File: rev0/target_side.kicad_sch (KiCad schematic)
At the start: 12 parts, among them IC1 ECP5-BGA256, U9 USB3343-CP

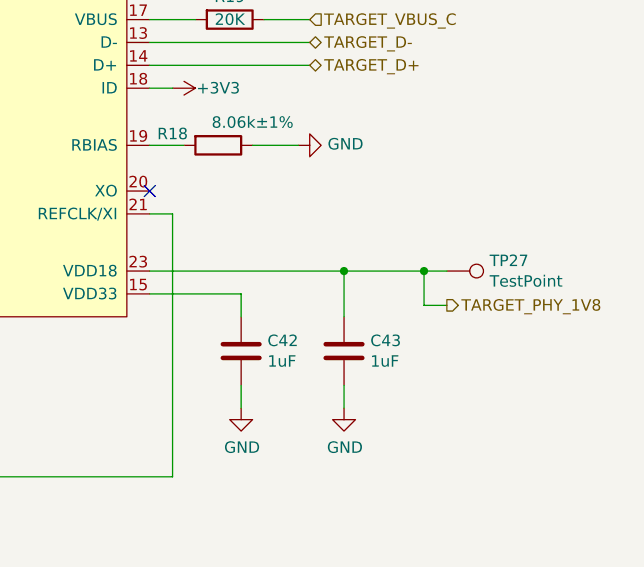
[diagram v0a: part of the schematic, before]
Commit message: hardware: remove PHY 1.8 V measurement
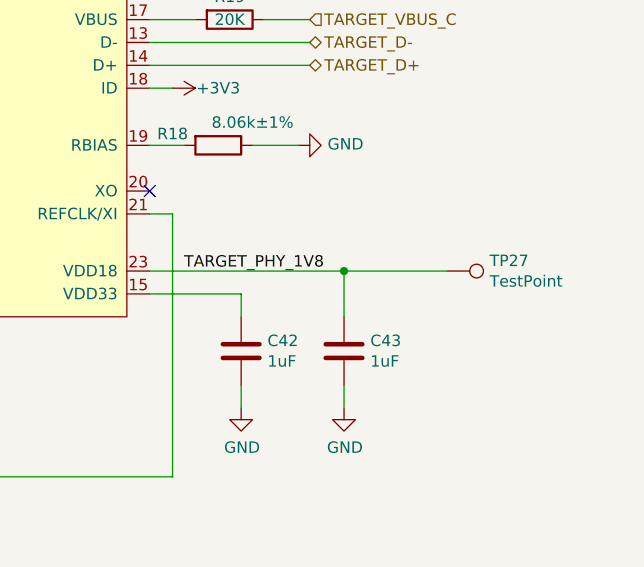
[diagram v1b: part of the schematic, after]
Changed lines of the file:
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@@
   (junction (at 123.19 66.04) (diameter 0) (color 0 0 0 0)
-  )
-  (junction (at 256.54 91.44) (diameter 0) (color 0 0 0 0)
   )
   (no_connect (at 59.69 99.06))
@@
     (stroke (width 0) (type default) (color 0 0 0 0))
   )
-  (wire (pts (xy 256.54 95.25) (xy 256.54 91.44))
-    (stroke (width 0) (type default) (color 0 0 0 0))
-  )
   (wire (pts (xy 59.69 91.44) (xy 137.16 91.44))
     (stroke (width 0) (type default) (color 0 0 0 0))
@@
     (stroke (width 0) (type default) (color 0 0 0 0))
   )
-  (wire (pts (xy 256.54 91.44) (xy 259.08 91.44))
-    (stroke (width 0) (type default) (color 0 0 0 0))
-  )
   (wire (pts (xy 59.69 124.46) (xy 137.16 124.46))
     (stroke (width 0) (type default) (color 0 0 0 0))
@@
     (stroke (width 0) (type default) (color 0 0 0 0))
   )
-  (wire (pts (xy 259.08 95.25) (xy 256.54 95.25))
-    (stroke (width 0) (type default) (color 0 0 0 0))
-  )
   (wire (pts (xy 226.06 91.44) (xy 247.65 91.44))
     (stroke (width 0) (type default) (color 0 0 0 0))
@@
     (stroke (width 0) (type default) (color 0 0 0 0))
   )
-  (wire (pts (xy 247.65 91.44) (xy 256.54 91.44))
+  (wire (pts (xy 247.65 91.44) (xy 259.08 91.44))
     (stroke (width 0) (type default) (color 0 0 0 0))
   )
@@
     (effects (font (size 1.27 1.27)) (justify left bottom))
   )
+  (label "TARGET_PHY_1V8" (at 229.87 91.44 0)
+    (effects (font (size 1.27 1.27)) (justify left bottom))
+  )
   (label "TARGET_DIR" (at 167.64 81.28 0)
     (effects (font (size 1.27 1.27)) (justify left bottom))
@@
     (effects (font (size 1.27 1.27)) (justify left))
   )
-  (hierarchical_label "TARGET_PHY_1V8" (shape output) (at 259.08 95.25 0)
-    (effects (font (size 1.27 1.27)) (justify left))
-  )

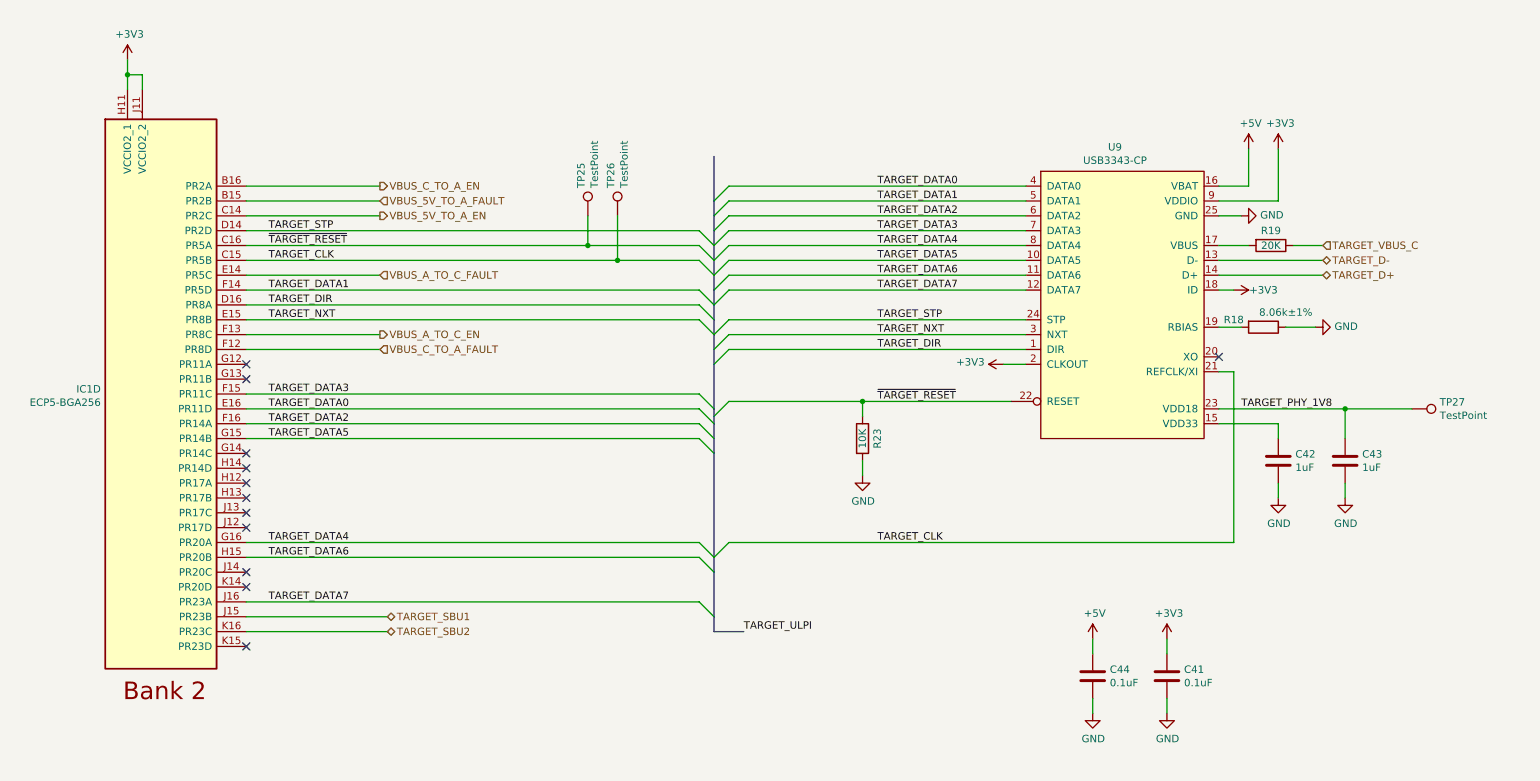
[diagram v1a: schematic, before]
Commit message: hardware: rename buses for KiCad 6
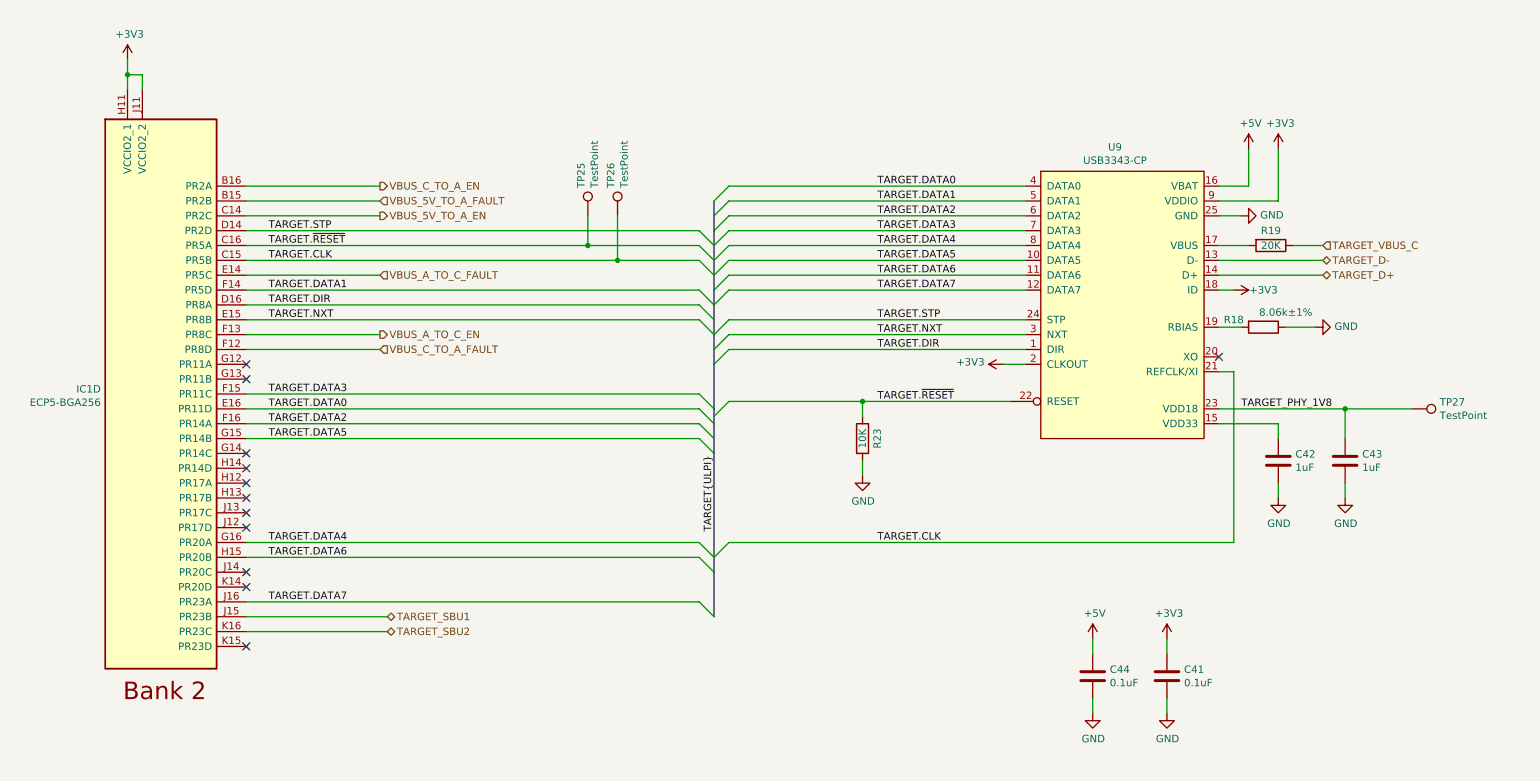
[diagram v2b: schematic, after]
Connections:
- net TARGET_CLK renamed TARGET.CLK
- net TARGET_DATA0 renamed TARGET.DATA0
- net TARGET_DATA1 renamed TARGET.DATA1
- net TARGET_DATA2 renamed TARGET.DATA2
- net TARGET_DATA3 renamed TARGET.DATA3
- net TARGET_DATA4 renamed TARGET.DATA4
- net TARGET_DATA5 renamed TARGET.DATA5
- net TARGET_DATA6 renamed TARGET.DATA6
- net TARGET_DATA7 renamed TARGET.DATA7
- net TARGET_DIR renamed TARGET.DIR
- net TARGET_NXT renamed TARGET.NXT
- net TARGET_STP renamed TARGET.STP
- net ~{TARGET_RESET} renamed TARGET.~{RESET}
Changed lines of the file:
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@@
-    (stroke (width 0) (type default) (color 0 0 0 0))
-  )
-  (bus (pts (xy 139.7 127) (xy 139.7 129.54))
     (stroke (width 0) (type default) (color 0 0 0 0))
   )
@@
     (stroke (width 0) (type default) (color 0 0 0 0))
   )
-  (bus (pts (xy 139.7 129.54) (xy 144.78 129.54))
-    (stroke (width 0) (type default) (color 0 0 0 0))
-  )
   (wire (pts (xy 193.04 68.58) (xy 142.24 68.58))
     (stroke (width 0) (type default) (color 0 0 0 0))
@@
     (stroke (width 0) (type default) (color 0 0 0 0))
   )
-  (bus (pts (xy 139.7 48.26) (xy 139.7 55.88))
-    (stroke (width 0) (type default) (color 0 0 0 0))
-  )
   (bus (pts (xy 139.7 92.71) (xy 139.7 93.98))
     (stroke (width 0) (type default) (color 0 0 0 0))
@@
     (stroke (width 0) (type default) (color 0 0 0 0))
   )
-  (label "TARGET_DATA2" (at 167.64 58.42 0)
-    (effects (font (size 1.27 1.27)) (justify left bottom))
-  )
-  (label "TARGET_STP" (at 63.5 60.96 0)
-    (effects (font (size 1.27 1.27)) (justify left bottom))
-  )
-  (label "TARGET_DATA3" (at 63.5 88.9 0)
-    (effects (font (size 1.27 1.27)) (justify left bottom))
-  )
-  (label "TARGET_DATA5" (at 167.64 66.04 0)
-    (effects (font (size 1.27 1.27)) (justify left bottom))
-  )
-  (label "TARGET_DATA0" (at 167.64 53.34 0)
-    (effects (font (size 1.27 1.27)) (justify left bottom))
-  )
-  (label "TARGET_DATA4" (at 63.5 114.3 0)
-    (effects (font (size 1.27 1.27)) (justify left bottom))
-  )
-  (label "TARGET_DATA5" (at 63.5 96.52 0)
-    (effects (font (size 1.27 1.27)) (justify left bottom))
-  )
-  (label "TARGET_CLK" (at 63.5 66.04 0)
-    (effects (font (size 1.27 1.27)) (justify left bottom))
-  )
-  (label "TARGET_DIR" (at 63.5 73.66 0)
-    (effects (font (size 1.27 1.27)) (justify left bottom))
-  )
-  (label "~{TARGET_RESET}" (at 167.64 90.17 0)
-    (effects (font (size 1.27 1.27)) (justify left bottom))
-  )
-  (label "TARGET_DATA1" (at 63.5 71.12 0)
-    (effects (font (size 1.27 1.27)) (justify left bottom))
-  )
-  (label "TARGET_CLK" (at 167.64 114.3 0)
-    (effects (font (size 1.27 1.27)) (justify left bottom))
-  )
-  (label "TARGET_ULPI" (at 144.78 129.54 0)
-    (effects (font (size 1.27 1.27)) (justify left bottom))
-  )
-  (label "TARGET_NXT" (at 167.64 78.74 0)
-    (effects (font (size 1.27 1.27)) (justify left bottom))
-  )
-  (label "TARGET_DATA6" (at 167.64 68.58 0)
-    (effects (font (size 1.27 1.27)) (justify left bottom))
-  )
-  (label "TARGET_DATA6" (at 63.5 116.84 0)
-    (effects (font (size 1.27 1.27)) (justify left bottom))
-  )
-  (label "TARGET_DATA7" (at 63.5 124.46 0)
-    (effects (font (size 1.27 1.27)) (justify left bottom))
-  )
-  (label "TARGET_DATA1" (at 167.64 55.88 0)
-    (effects (font (size 1.27 1.27)) (justify left bottom))
-  )
-  (label "~{TARGET_RESET}" (at 63.5 63.5 0)
-    (effects (font (size 1.27 1.27)) (justify left bottom))
-  )
-  (label "TARGET_DATA4" (at 167.64 63.5 0)
-    (effects (font (size 1.27 1.27)) (justify left bottom))
-  )
-  (label "TARGET_NXT" (at 63.5 76.2 0)
+  (label "TARGET.DATA2" (at 167.64 58.42 0)
+    (effects (font (size 1.27 1.27)) (justify left bottom))
+  )
+  (label "TARGET.STP" (at 63.5 60.96 0)
+    (effects (font (size 1.27 1.27)) (justify left bottom))
+  )
+  (label "TARGET.DATA3" (at 63.5 88.9 0)
+    (effects (font (size 1.27 1.27)) (justify left bottom))
+  )
+  (label "TARGET.DATA5" (at 167.64 66.04 0)
+    (effects (font (size 1.27 1.27)) (justify left bottom))
+  )
+  (label "TARGET.DATA0" (at 167.64 53.34 0)
+    (effects (font (size 1.27 1.27)) (justify left bottom))
+  )
+  (label "TARGET.DATA4" (at 63.5 114.3 0)
+    (effects (font (size 1.27 1.27)) (justify left bottom))
+  )
+  (label "TARGET.DATA5" (at 63.5 96.52 0)
+    (effects (font (size 1.27 1.27)) (justify left bottom))
+  )
+  (label "TARGET.CLK" (at 63.5 66.04 0)
+    (effects (font (size 1.27 1.27)) (justify left bottom))
+  )
+  (label "TARGET.DIR" (at 63.5 73.66 0)
+    (effects (font (size 1.27 1.27)) (justify left bottom))
+  )
+  (label "TARGET.~{RESET}" (at 167.64 90.17 0)
+    (effects (font (size 1.27 1.27)) (justify left bottom))
+  )
+  (label "TARGET.DATA1" (at 63.5 71.12 0)
+    (effects (font (size 1.27 1.27)) (justify left bottom))
+  )
+  (label "TARGET.CLK" (at 167.64 114.3 0)
+    (effects (font (size 1.27 1.27)) (justify left bottom))
+  )
+  (label "TARGET.NXT" (at 167.64 78.74 0)
+    (effects (font (size 1.27 1.27)) (justify left bottom))
+  )
+  (label "TARGET.DATA6" (at 167.64 68.58 0)
+    (effects (font (size 1.27 1.27)) (justify left bottom))
+  )
+  (label "TARGET.DATA6" (at 63.5 116.84 0)
+    (effects (font (size 1.27 1.27)) (justify left bottom))
+  )
+  (label "TARGET.DATA7" (at 63.5 124.46 0)
+    (effects (font (size 1.27 1.27)) (justify left bottom))
+  )
+  (label "TARGET.DATA1" (at 167.64 55.88 0)
+    (effects (font (size 1.27 1.27)) (justify left bottom))
+  )
+  (label "TARGET.~{RESET}" (at 63.5 63.5 0)
+    (effects (font (size 1.27 1.27)) (justify left bottom))
+  )
+  (label "TARGET.DATA4" (at 167.64 63.5 0)
+    (effects (font (size 1.27 1.27)) (justify left bottom))
+  )
+  (label "TARGET.NXT" (at 63.5 76.2 0)
     (effects (font (size 1.27 1.27)) (justify left bottom))
   )
@@
     (effects (font (size 1.27 1.27)) (justify left bottom))
   )
-  (label "TARGET_DIR" (at 167.64 81.28 0)
-    (effects (font (size 1.27 1.27)) (justify left bottom))
-  )
-  (label "TARGET_DATA7" (at 167.64 71.12 0)
-    (effects (font (size 1.27 1.27)) (justify left bottom))
-  )
-  (label "TARGET_DATA2" (at 63.5 93.98 0)
-    (effects (font (size 1.27 1.27)) (justify left bottom))
-  )
-  (label "TARGET_STP" (at 167.64 76.2 0)
-    (effects (font (size 1.27 1.27)) (justify left bottom))
-  )
-  (label "TARGET_DATA0" (at 63.5 91.44 0)
-    (effects (font (size 1.27 1.27)) (justify left bottom))
-  )
-  (label "TARGET_DATA3" (at 167.64 60.96 0)
-    (effects (font (size 1.27 1.27)) (justify left bottom))
-  )
+  (label "TARGET.DIR" (at 167.64 81.28 0)
+    (effects (font (size 1.27 1.27)) (justify left bottom))
+  )
+  (label "TARGET.DATA7" (at 167.64 71.12 0)
+    (effects (font (size 1.27 1.27)) (justify left bottom))
+  )
+  (label "TARGET.DATA2" (at 63.5 93.98 0)
+    (effects (font (size 1.27 1.27)) (justify left bottom))
+  )
+  (label "TARGET{ULPI}" (at 139.7 112.395 90)
+    (effects (font (size 1.27 1.27)) (justify left bottom))
+  )
+  (label "TARGET.STP" (at 167.64 76.2 0)
+    (effects (font (size 1.27 1.27)) (justify left bottom))
+  )
+  (label "TARGET.DATA0" (at 63.5 91.44 0)
+    (effects (font (size 1.27 1.27)) (justify left bottom))
+  )
+  (label "TARGET.DATA3" (at 167.64 60.96 0)
+    (effects (font (size 1.27 1.27)) (justify left bottom))
+  )

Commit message: hardware: use DNP field for DNP notation
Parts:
- TP25, TP26, TP27: DNP (none) -> DNP; Note DNP -> (none)
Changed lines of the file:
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@@
       (effects (font (size 1.27 1.27)) hide)
     )
-    (property "Note" "DNP" (id 4) (at 259.08 91.44 0)
+    (property "DNP" "DNP" (id 4) (at 259.08 91.44 0)
       (effects (font (size 1.27 1.27)) hide)
     )
@@
       (effects (font (size 1.27 1.27)) hide)
     )
-    (property "Note" "DNP" (id 4) (at 118.11 58.42 0)
+    (property "DNP" "DNP" (id 4) (at 118.11 58.42 0)
       (effects (font (size 1.27 1.27)) hide)
     )
@@
       (effects (font (size 1.27 1.27)) hide)
     )
-    (property "Note" "DNP" (id 4) (at 123.19 58.42 0)
+    (property "DNP" "DNP" (id 4) (at 123.19 58.42 0)
       (effects (font (size 1.27 1.27)) hide)
     )

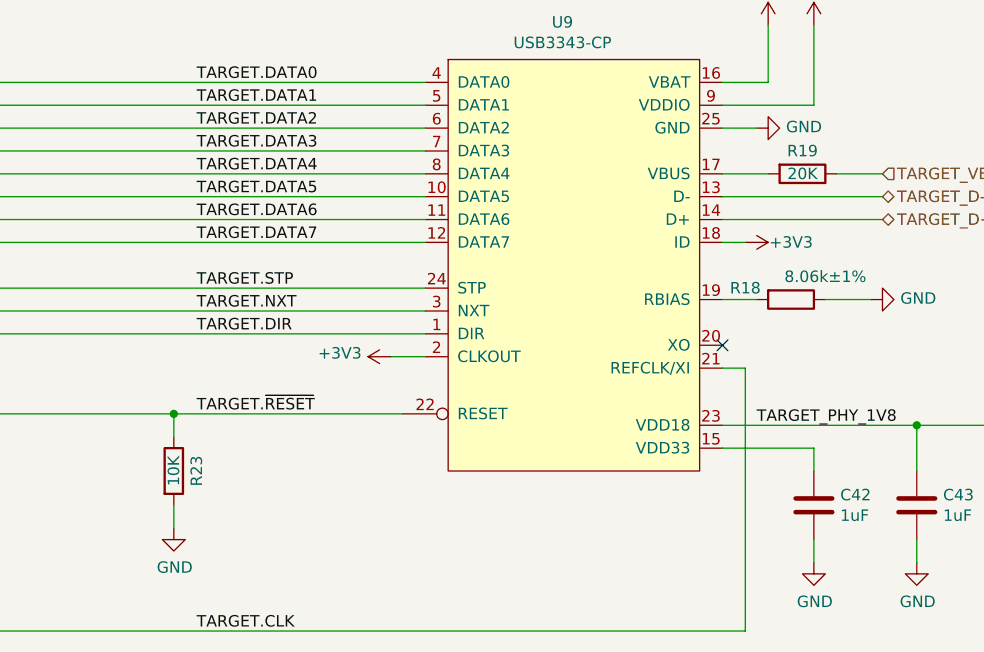
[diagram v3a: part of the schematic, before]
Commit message: hardware: consistently use lowercase k for kilo
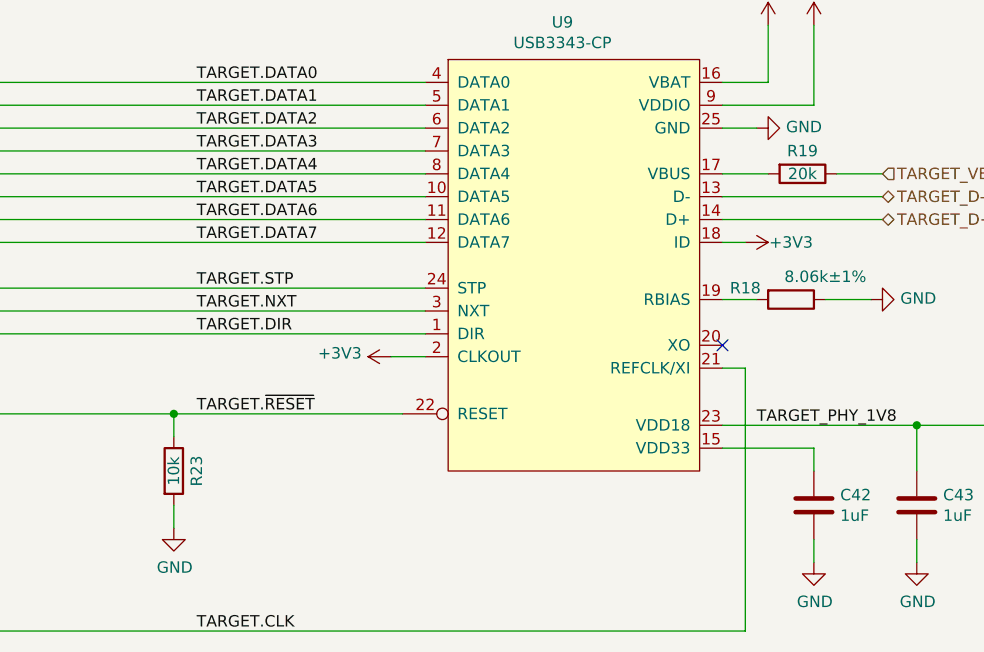
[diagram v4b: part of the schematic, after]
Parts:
- R19: value 20K -> 20k
- R23: value 10K -> 10k
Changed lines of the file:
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@@
     (in_bom yes) (on_board yes)
     (property "Reference" "R19" (id 0) (at 234.95 60.96 90))
-    (property "Value" "20K" (id 1) (at 234.95 63.5 90))
+    (property "Value" "20k" (id 1) (at 234.95 63.5 90))
     (property "Footprint" "Resistor_SMD:R_0402_1005Metric" (id 2) (at 234.95 61.722 90)
       (effects (font (size 1.27 1.27)) hide)
@@
     (in_bom yes) (on_board yes)
     (property "Reference" "R23" (id 0) (at 167.64 96.52 90))
-    (property "Value" "10K" (id 1) (at 165.1 96.52 90))
+    (property "Value" "10k" (id 1) (at 165.1 96.52 90))
     (property "Footprint" "Resistor_SMD:R_0402_1005Metric" (id 2) (at 163.322 96.52 90)
       (effects (font (size 1.27 1.27)) hide)
